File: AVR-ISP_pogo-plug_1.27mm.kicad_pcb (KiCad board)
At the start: 2 copper layers, 12 x 19 mm, 4 parts, among them P1 CONN_6, P2 CONN_6

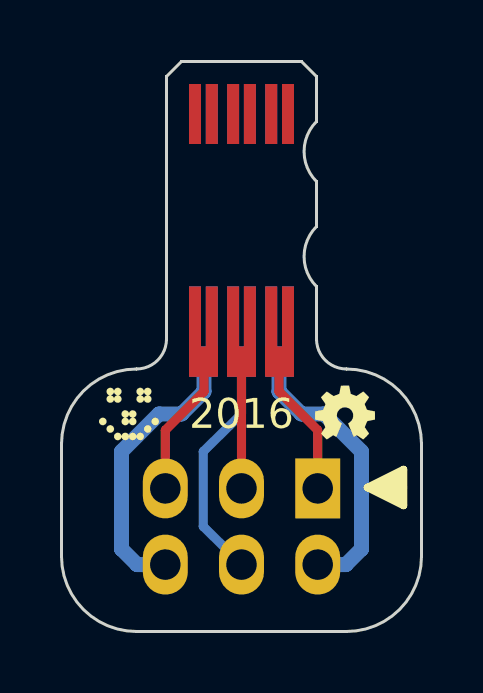
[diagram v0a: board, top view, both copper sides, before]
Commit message: Add curved edges for better ergonomics
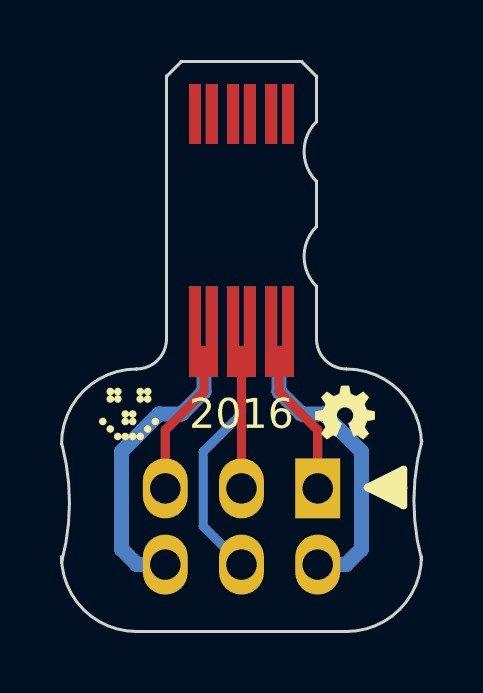
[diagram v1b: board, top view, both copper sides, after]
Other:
- outline, holes or cut-outs redrawn
